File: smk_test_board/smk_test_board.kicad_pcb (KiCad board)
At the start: 2 copper layers, 76 x 113.2 mm, 50 parts, among them J1 Battery JST-SH, J2 BAT+ / BAT- flying leads, SW00 KS-2P02B01-02, SW01 KS-2P02B01-02, SW10 KS-2P02B01-02, SW11 KS-2P02B01-02, SW12 KS-2P02B01-02, SW20 KS-2P02B01-02, SW21 KS-2P02B01-02, SW22 KS-2P02B01-02, U1 XIAO_ESP32C6, U2 SN74AHCT1G125DBVR

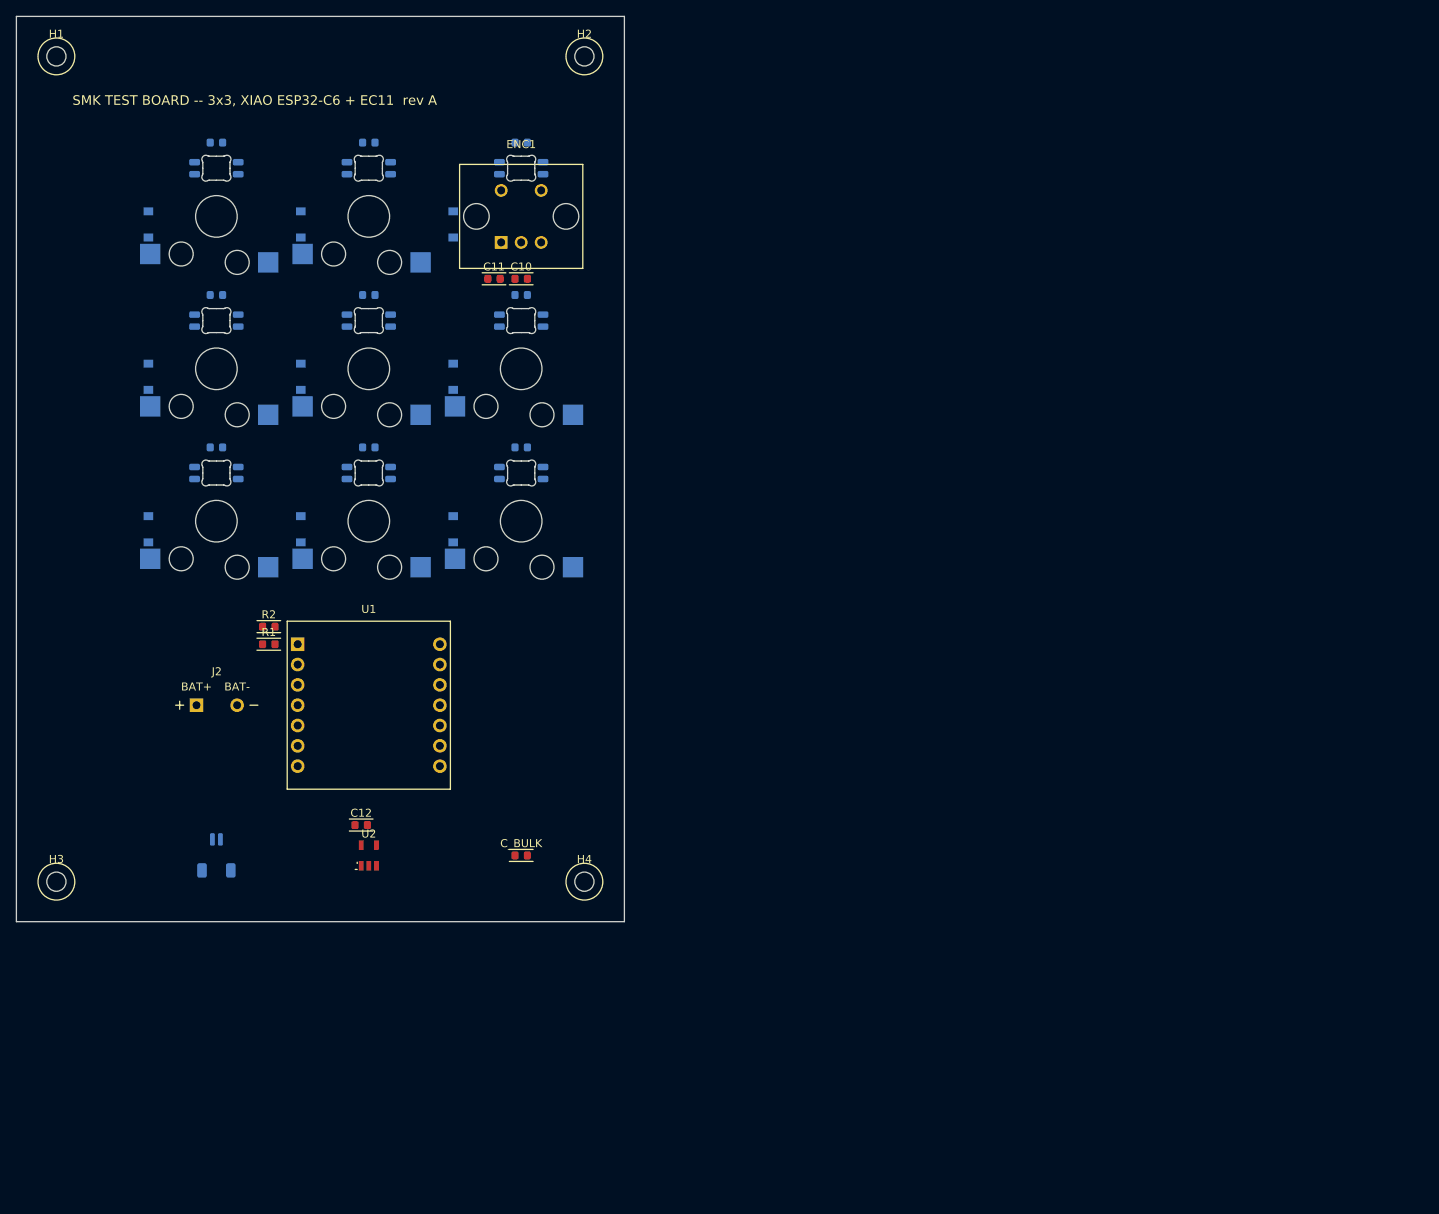
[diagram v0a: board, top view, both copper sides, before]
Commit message: Route the board: router.py generates the copper; shrink to 65.7 x 91.73 mm
router.py rasterises every obstacle onto a 0.2 mm grid and routes with an
8-direction A* (turn and via costs), shortest MST edge first; GND is a pour
on both layers with a stub via per pad. The outline is now derived from the
placement. DRC with --refill-zones: 16 errors / 0 unconnected, as unrouted.
28 tests pass.

Co-Authored-By: Claude Opus 5.5 <noreply@anthropic.com>
Claude-Session: https://claude.ai/code/session_01PWVS4DMn5rniJecYgbPE6J
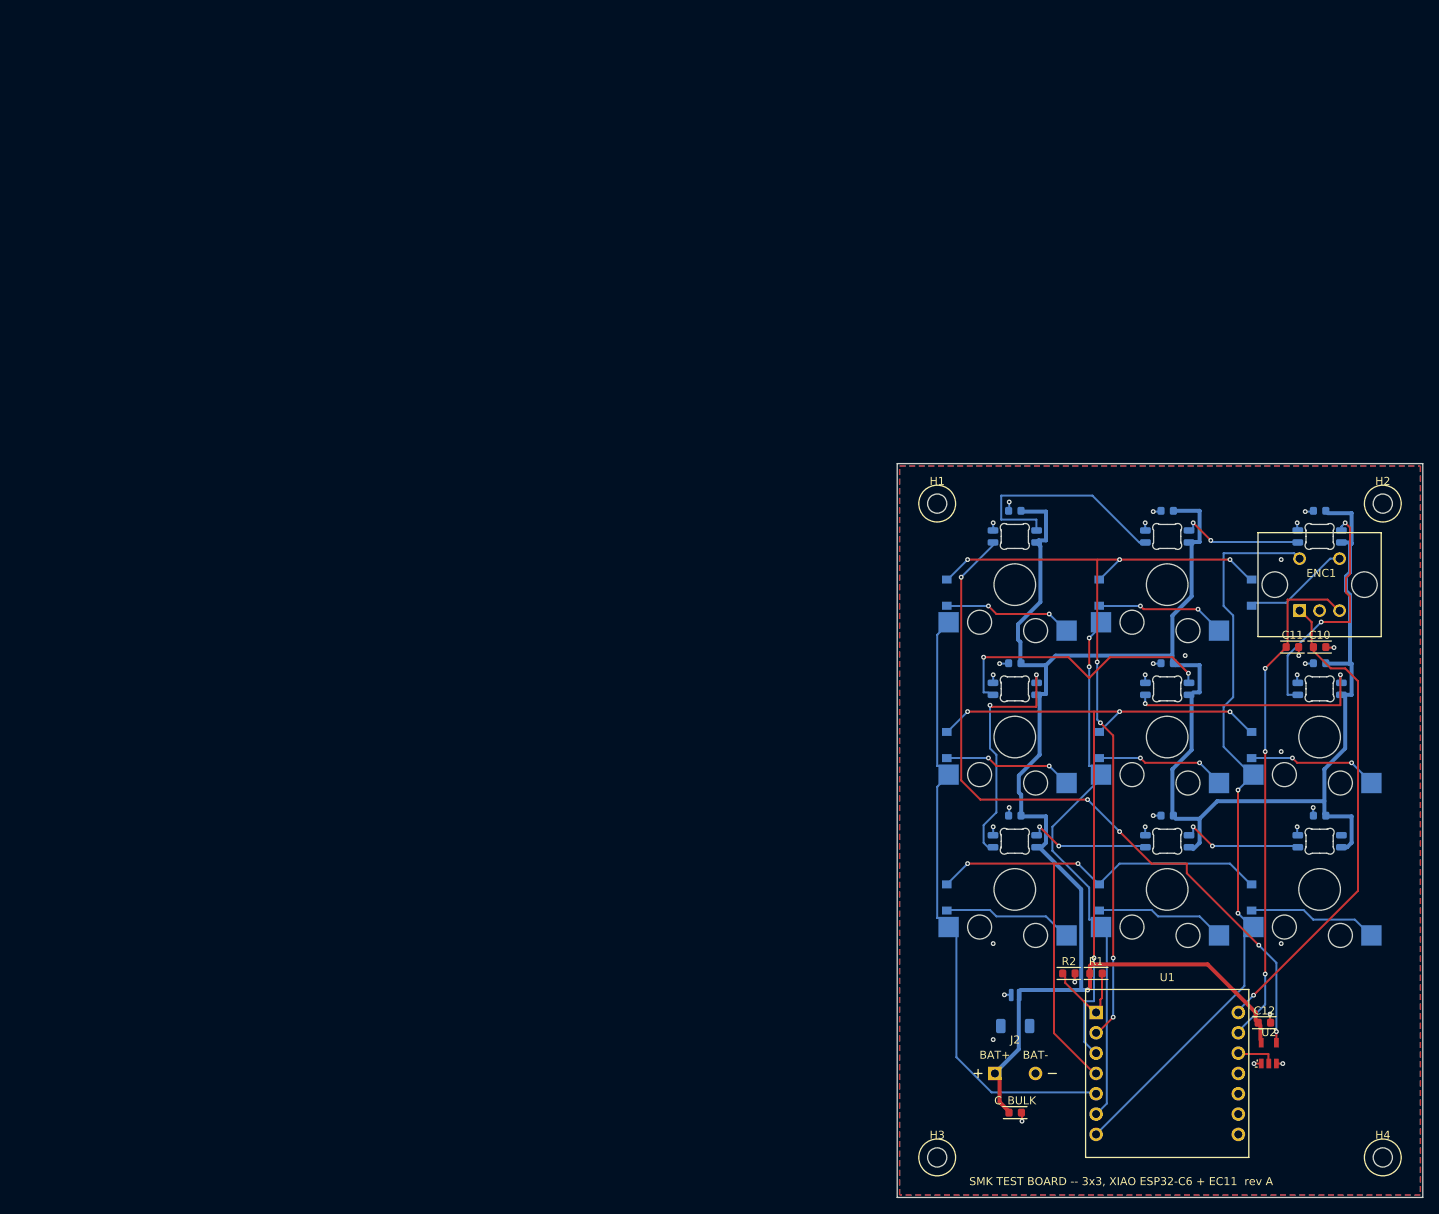
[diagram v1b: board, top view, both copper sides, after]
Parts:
- moved H1 123.5 mm to (115.1, 60.9)
- moved C12 115.6 mm to (156.0, 125.8)
- moved H3 115.4 mm to (115.1, 142.6)
- moved U2 115.2 mm to (156.6, 129.6)
- moved H2 114.4 mm to (170.8, 60.9)
- moved R1 111.3 mm to (135.0, 119.6)
- moved C10 109.9 mm to (162.9, 78.8)
- moved C3 109.9 mm to (162.9, 61.8)
- moved C4 109.9 mm to (162.9, 80.9)
- moved C9 109.9 mm to (162.9, 99.9)
- moved D02 109.9 mm to (154.4, 72.0)
- moved D12 109.9 mm to (154.4, 91.1)
- moved D22 109.9 mm to (154.4, 110.1)
- moved ENC1 109.9 mm to (162.9, 71.0)
- moved RGB3 109.9 mm to (162.9, 65.0)
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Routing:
- net VSYS: track 0.00 -> 269.9 mm, vias 0 -> 1
- net ROW0: track 0.00 -> 102.4 mm, vias 0 -> 7
- net LEDD1: track 0.00 -> 90.5 mm, vias 0 -> 5
- net COL2: track 0.00 -> 88.8 mm, vias 0 -> 2
- net ROW1: track 0.00 -> 86.7 mm, vias 0 -> 4
- net ROW2: track 0.00 -> 68.6 mm, vias 0 -> 2
- net COL0: track 0.00 -> 68.6 mm
- net ENC_B: track 0.00 -> 61.7 mm, vias 0 -> 3
- net COL1: track 0.00 -> 61.2 mm, vias 0 -> 2
- net ENC_A: track 0.00 -> 58.2 mm, vias 0 -> 1
- net LEDD6: track 0.00 -> 34.6 mm, vias 0 -> 2
- net LEDD4: track 0.00 -> 29.9 mm, vias 0 -> 2
- net LEDD5: track 0.00 -> 29.9 mm, vias 0 -> 2
- net LEDD7: track 0.00 -> 29.7 mm, vias 0 -> 2
- net LEDD2: track 0.00 -> 29.2 mm
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- added copper zone on B.Cu, net GND
- added copper zone on F.Cu, net GND
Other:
- board size 76 x 113.2 mm -> 65.7 x 91.7 mm
